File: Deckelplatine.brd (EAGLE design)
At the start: 160 x 100 mm, 57 parts, among them IC1 MAX481CSA, IC2 74HCT595D, IC3 74HCT595D, IC4 74HCT595D, IC5 74HCT595D, IC6 74HCT595D, J1 CON25, U1 LM2676S, X1 ''

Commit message: Begin mit dem Board Layout
Erste Lieferung von Farnell angekommen.
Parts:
- J1: value CON25 -> 52808-2570; device RA-GAS Projekte LTD:CON25 -> RA-GAS Projekte LTD:52808-2570
- moved R2 172.9 mm to (93.0, 7.00), turned to 90 degrees
- moved IC1 159.9 mm to (83.1, 69.0), turned to 270 degrees
- moved R4 159.3 mm to (70.9, 4.42), turned to 180 degrees
- moved C4 153.1 mm to (91.1, 29.2)
- moved D2 147.7 mm to (71.2, 13.9), turned to 90 degrees
- moved X1 146.6 mm to (103.4, 10.3), turned to 270 degrees
- moved F1 135.1 mm to (101.6, 29.2), turned to 270 degrees
- moved D1 133.4 mm to (64.5, 15.8), turned to 180 degrees
- moved IC3 132.4 mm to (68.5, 65.3), turned to 90 degrees
- moved JP3 131.5 mm to (104.1, 58.9), turned to 90 degrees
- moved R1 124.8 mm to (93.0, 12.8), turned to 90 degrees
- moved R15 123.2 mm to (40.0, 30.5), turned to 90 degrees
- moved JP2 122.2 mm to (95.3, 67.4)
- moved R14 118.2 mm to (41.0, 34.0), turned to 90 degrees
- moved IC2 115.9 mm to (68.5, 53.5), turned to 90 degrees
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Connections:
- net BETRIEB: now also J1.21; no longer J1.P$21
- net BLINK: now also J1.24; no longer J1.P$24
- net D1: now also J1.1; no longer J1.P$1
- net D17: now also J1.17; no longer J1.P$17
- net D18: now also J1.18; no longer J1.P$18
- net D19: now also J1.19; no longer J1.P$19
- net D2: now also J1.2; no longer J1.P$2
- net D20: now also J1.20; no longer J1.P$20
- net D3: now also J1.3; no longer J1.P$3
- net D4: now also J1.4; no longer J1.P$4
- net D5: now also J1.5; no longer J1.P$5
- net D6: now also J1.6; no longer J1.P$6
- net D7: now also J1.7; no longer J1.P$7
- net D8: now also J1.8; no longer J1.P$8
- net GND: now also J1.25; no longer J1.P$25
- net N$31: now also J1.9; no longer J1.P$9
- net N$32: now also J1.10; no longer J1.P$10
- net N$33: now also J1.11; no longer J1.P$11
- net N$34: now also J1.12; no longer J1.P$12
- net N$35: now also J1.13; no longer J1.P$13
- net N$36: now also J1.14; no longer J1.P$14
- net N$37: now also J1.15; no longer J1.P$15
- net N$38: now also J1.16; no longer J1.P$16
- net STOERUNG: now also J1.22; no longer J1.P$22
- net WARTUNG: now also J1.23; no longer J1.P$23
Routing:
- net TXD: track 0.00 -> 130.1 mm
- net MON_MAINS: track 0.00 -> 101.4 mm
- net 12V_VIN: track 0.00 -> 12.4 mm
- net GND: track 0.00 -> 1.03 mm
- net VCC: track 0.00 -> 0.56 mm
- added copper zone on layer 1, net GND
- added copper zone on layer 16, net GND
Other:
- board size 160 x 100 mm -> 110 x 75 mm

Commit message: Stromlaufplan fast fertig.
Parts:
- added X2: 233-502, con-wago_233:P-233-502
- C1, C10, C7, C8, C9: device rcl:C1206 -> resistor:C0603
- C11: value 0.1uF -> 100n; device rcl:C1206 -> resistor:C0603
- C4: value 0.01uF -> 0.1uF; device rcl:C0805 -> rcl:C1206
- C5: value 100uF 16v -> 0.01uF; device rcl:PANASONIC_D -> rcl:C0805
- C6: value 100n -> 100uF 16v; device rcl:C1206 -> rcl:PANASONIC_D
- F1: device fuse:KS9V -> fuse-schurter:3101.0040
- IC1: value MAX481CSA -> MAX1487EESA+
- JP1: value CON6 -> ''
- L1: value 09HCP33UH -> DO5022P-EU_; device Inductor-Fastron:09HCP -> RA-GAS Projekte LTD:DO5022P
- X1: value '' -> 236-404; device con-wago:233-504 -> con-wago_236:P-236-404
- moved C1 83.4 mm to (92.8, 61.0), turned to 0 degrees
- moved C7 82.9 mm to (74.7, 72.2), turned to 0 degrees
- moved C3 67.4 mm to (85.0, 25.0), turned to 270 degrees
- moved C2 65.4 mm to (88.0, 25.0), turned to 270 degrees
- moved R2 65.1 mm to (28.0, 4.00)
- moved R1 65.0 mm to (28.0, 11.0)
- moved IC3 55.1 mm to (13.4, 66.7), turned to 270 degrees
- moved C8 48.9 mm to (73.9, 59.2), turned to 0 degrees
- moved IC2 46.0 mm to (24.4, 66.5), turned to 270 degrees
- moved C6 40.5 mm to (56.3, 19.0)
- moved R4 36.9 mm to (34.0, 4.00), turned to 90 degrees
- moved R3 31.5 mm to (34.0, 11.0), turned to 90 degrees
- moved C11 28.4 mm to (27.0, 31.0), turned to 270 degrees
- moved U1 28.2 mm to (87.9, 44.0), turned to 270 degrees
- moved F1 23.4 mm to (83.6, 14.2)
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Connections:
- net BETRIEB renamed D21
- net BLINK renamed D24
- net N$31 renamed D9
- net N$32 renamed D10
- net N$33 renamed D11
- net N$34 renamed D12
- net N$35 renamed D13
- net N$36 renamed D14
- net N$37 renamed D15
- net N$38 renamed D16
- net STOERUNG renamed D22
- net WARTUNG renamed D23
- new net N$31: F1.3, F1.4
- net 12V_VIN: now also C4.1, X1.L1.1, X1.L1.2; no longer C11.1, X1.B1
- net ACCU+: now also F1.2, X1.L3.1, X1.L3.2; no longer X1.B3
- net ACCU-: now also X1.L4.1, X1.L4.2; no longer X1.B4
- net GND: now also C4.2, C6.-, X1.L2.1, X1.L2.2, X2.L2.1, X2.L2.2; no longer C5.-, C6.2, X1.B2
- net N$1: no longer F1.2
- net N$42: now also C5.2; no longer C4.2
- net N$44: now also C5.1, L1.1; no longer C4.1, L1.P$2
- net VCC: now also C11.1, C6.+, L1.2, X2.L1.1, X2.L1.2; no longer C5.+, C6.1, L1.P$1
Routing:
- net TXD: track 130.1 -> 0.00 mm
- net MON_MAINS: track 101.4 -> 0.00 mm
- net 12V_VIN: track 12.4 -> 0.00 mm
- net VCC: track 0.56 -> 0.00 mm

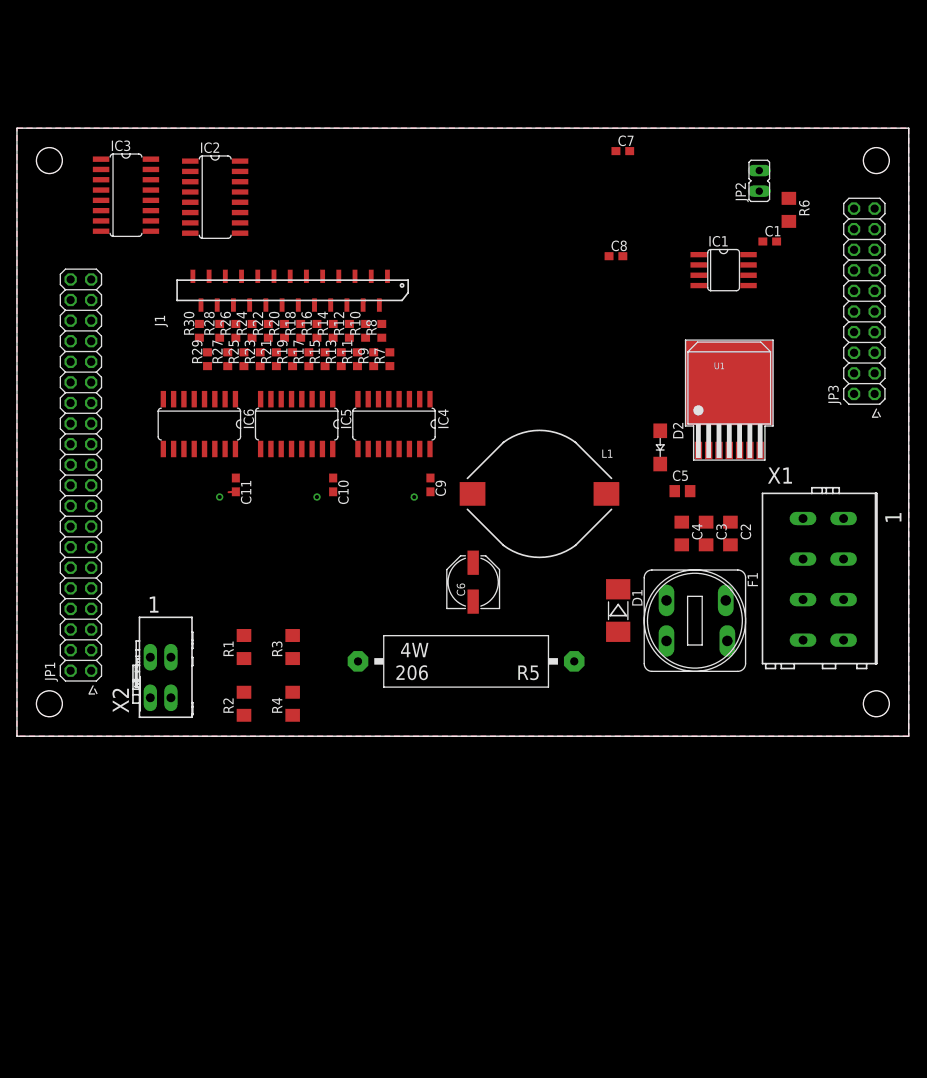
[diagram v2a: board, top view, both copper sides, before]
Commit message: Schema mit Verpolschutz an Vin und Accu.
Schaltregler nach Application Note von Texas Instruments.
Eingänge für den MON_MAINS und MON_BAT (GPIO Banana Pro Eingänge zur Überwachung Vin und Accu) sind durch NPN Transistoren gegen Überspannunge geschützt
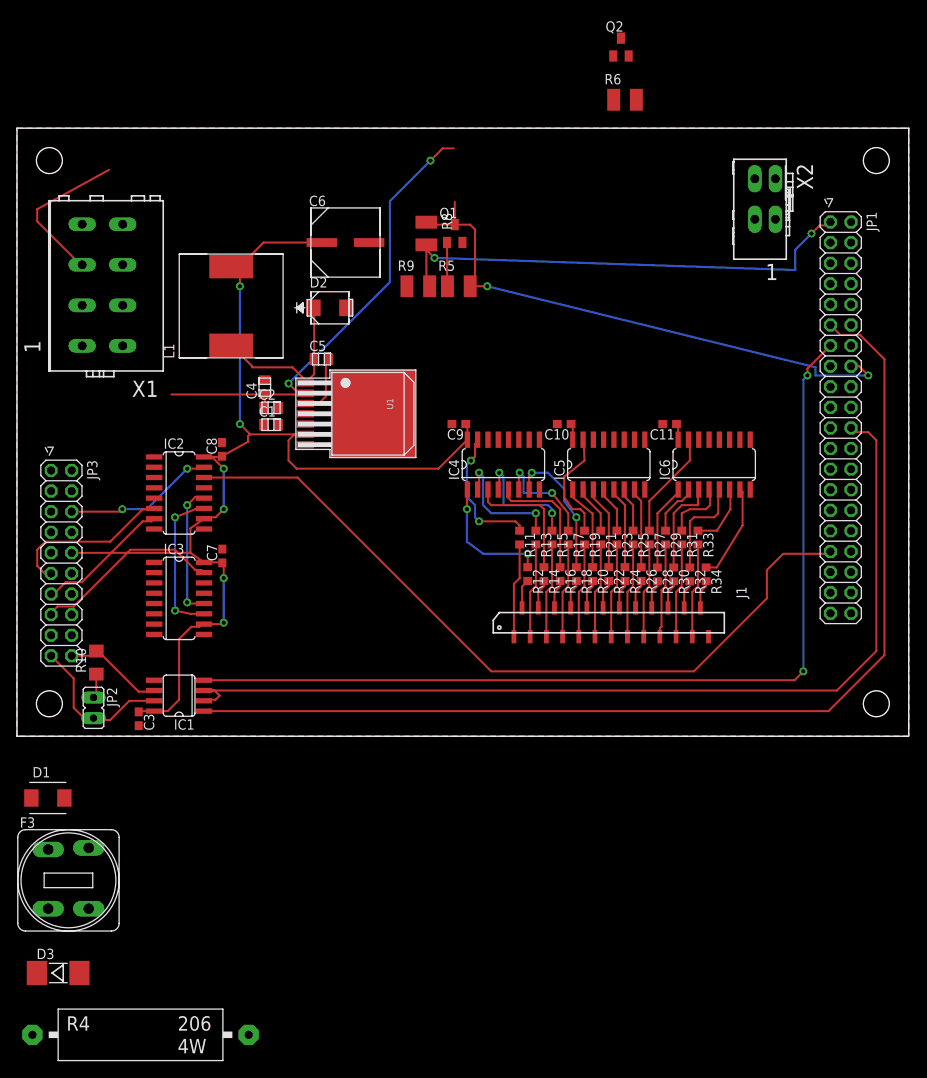
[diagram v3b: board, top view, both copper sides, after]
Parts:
- removed F1: 0.63AT, fuse-schurter:3101.0040
- removed R1, R3: 20k, rcl:R1206
- removed R2: 3.3k, rcl:R1206
- removed R7: 2.2k, RA-GAS Projekte LTD:R0603
- added D3: LL4005G, diode:MELF-MLL41
- added F3: 0.63AT, fuse-schurter:3101.0040
- added Q1, Q2: BC846BSMD, transistor-npn:SOT23
- added R31, R32, R33, R34: 2.2k, RA-GAS Projekte LTD:R0603
- C1: value 100n -> 0.1uF; device resistor:C0603 -> AcceleratedDesigns_Lib:GRM21BR61E475MA12L
- C2: device rcl:C1206 -> AcceleratedDesigns_Lib:GRM21BR61E475MA12L
- C3: value 0.1uF -> 100n; device rcl:C1206 -> resistor:C0603
- C4: device rcl:C1206 -> AcceleratedDesigns_Lib:0805
- C5: device rcl:C0805 -> AcceleratedDesigns_Lib:GRM216R71H103KA01D
- C6: device rcl:PANASONIC_D -> AcceleratedDesigns_Lib:SM_RADIAL_8MM
- D1: value LL4005G -> (none); device diode:MELF-MLL41 -> diode:SMBJ
- D2: value GF1 -> 450mV; device diode:SMA-DO214AC -> AcceleratedDesigns_Lib:SMB
- L1: value DO5022P-EU_ -> SRR1280-150M; device RA-GAS Projekte LTD:DO5022P -> AcceleratedDesigns_Lib:SRR1280
- R10: value 2.2k -> 120R; device RA-GAS Projekte LTD:R0603 -> rcl:R1206
- R4: value 3.3k -> 150R RMO3E150; device rcl:R1206 -> resistor-power:KH206-8
- R5: value 150R RMO3E150 -> 1k; device resistor-power:KH206-8 -> rcl:R1210
- R6: value 120R -> 1k; device rcl:R1206 -> rcl:R1210
- R8, R9: value 2.2k -> 10k; device RA-GAS Projekte LTD:R0603 -> rcl:R1210
- moved JP2 104.7 mm to (9.44, 3.50), turned to 180 degrees
- moved JP3 104.2 mm to (5.48, 21.4), turned to 270 degrees
- moved X1 95.1 mm to (11.0, 55.5), turned to 180 degrees
- moved JP1 94.0 mm to (101.6, 39.3), turned to 270 degrees
- moved X2 93.1 mm to (92.0, 65.0), turned to 270 degrees
- moved IC1 85.2 mm to (20.0, 5.00), turned to 90 degrees
- moved D1 74.1 mm to (3.81, -7.62), turned to 0 degrees
- moved C3 73.6 mm to (15.0, 2.15)
- moved C7 70.2 mm to (25.3, 22.2), turned to 90 degrees
- moved R30 65.8 mm to (81.0, 20.0), turned to 270 degrees
- moved C1 65.5 mm to (31.3, 38.4)
- moved IC6 63.7 mm to (86.0, 33.5), turned to 0 degrees
- moved R28 61.8 mm to (79.0, 20.0), turned to 270 degrees
- moved R29 60.6 mm to (80.0, 24.5), turned to 270 degrees
- moved C2 58.7 mm to (31.3, 40.5), turned to 0 degrees
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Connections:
- removed net MON_BAT: JP1.18, R3.1, R4.2
- removed net MON_MAINS: JP1.16, R1.1, R2.2
- removed net N$1: D1.A, R3.2, R5.1
- removed net N$31: F1.3, F1.4
- new net !MON_BAT: JP1.18, Q2.3, R6.2, R9.1
- new net !MON_MAINS: JP1.16, Q1.3, R5.2, R8.1
- new net N$37: Q1.1, R5.1
- new net N$38: D3.A, F3.4, R4.1
- new net N$39: F3.1
- new net N$4: Q2.1, R6.1
- new net V+: D3.C, R4.2
- net 12V_VIN: now also C1.1, D1.A; no longer C3.1, R1.2, R5.2
- net A-: now also R10.2; no longer R6.2
- net ACCU+: no longer F1.1, F1.2
- net ACCU-: no longer R4.1
- net D1: now also R11.2; no longer R7.2
- net D10: now also R20.2; no longer R16.2
- net D11: now also R21.2; no longer R17.2
- net D12: now also R22.2; no longer R18.2
- net D13: now also R23.2; no longer R19.2
- net D14: now also R24.2; no longer R20.2
- net D15: now also R25.2; no longer R21.2
- net D16: now also R26.2; no longer R22.2
- net D17: now also R27.2; no longer R23.2
- net D18: now also R28.2; no longer R24.2
- net D19: now also R29.2; no longer R25.2
- net D2: now also R12.2; no longer R8.2
- net D20: now also R30.2; no longer R26.2
- net D21: now also R31.2; no longer R27.2
- net D22: now also R32.2; no longer R28.2
- net D23: now also R33.2; no longer R29.2
- net D24: now also R34.2; no longer R30.2
- net D3: now also R13.2; no longer R9.2
- net D4: now also R14.2; no longer R10.2
- net D5: now also R15.2; no longer R11.2
- net D6: now also R16.2; no longer R12.2
- net D7: now also R17.2; no longer R13.2
- net D8: now also R18.2; no longer R14.2
- net D9: now also R19.2; no longer R15.2
- net GND: now also C6.2, D2.2, Q1.2, Q2.2; no longer C6.-, D2.A, R2.1
- net N$10: now also R15.1; no longer R11.1
- net N$11: now also R16.1; no longer R12.1
- net N$12: now also R17.1; no longer R13.1
- net N$13: now also R18.1; no longer R14.1
- net N$14: now also R19.1; no longer R15.1
- net N$15: now also R20.1; no longer R16.1
- net N$16: now also R21.1; no longer R17.1
- net N$17: now also R22.1; no longer R18.1
- net N$18: now also R10.1; no longer R6.1
- net N$19: now also R23.1; no longer R19.1
- net N$20: now also R24.1; no longer R20.1
- net N$21: now also R25.1; no longer R21.1
- net N$22: now also R26.1; no longer R22.1
- net N$23: now also R27.1; no longer R23.1
- net N$24: now also R28.1; no longer R24.1
- net N$25: now also R29.1; no longer R25.1
- net N$26: now also R30.1; no longer R26.1
- net N$27: now also R31.1; no longer R27.1
- net N$28: now also R32.1; no longer R28.1
- net N$29: now also R33.1; no longer R29.1
- net N$30: now also R34.1; no longer R30.1
- net N$44: now also D2.1; no longer D2.K
- net N$6: now also R11.1; no longer R7.1
- net N$7: now also R12.1; no longer R8.1
- net N$8: now also R13.1; no longer R9.1
- net N$9: now also R14.1; no longer R10.1
- net VCC: now also C3.1, C6.1; no longer C1.1, C6.+
- net VCC3.3V: now also R8.2, R9.2
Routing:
- net VCC: track 0.00 -> 144.8 mm, vias 0 -> 6
- net RXD: track 0.00 -> 131.7 mm
- net RTS: track 0.00 -> 118.9 mm
- net TXD: track 0.00 -> 115.9 mm, vias 0 -> 2
- net REL_SER: track 0.00 -> 95.3 mm
- net !MON_MAINS: track 0.00 -> 70.3 mm, vias 0 -> 2
- net VCC3.3V: track 0.00 -> 60.1 mm, vias 0 -> 2
- net 12V_VIN: track 0.00 -> 58.9 mm, vias 0 -> 2
- net P9: track 0.00 -> 23.5 mm
- net N$44: track 0.00 -> 21.1 mm
- net P7: track 0.00 -> 20.6 mm
- net ACCU+: track 0.00 -> 19.6 mm
- net B+: track 0.00 -> 19.1 mm
- net REL_SCK: track 0.00 -> 18.9 mm, vias 0 -> 2
- net P1: track 0.00 -> 18.6 mm, vias 0 -> 2
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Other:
- outline, holes or cut-outs redrawn

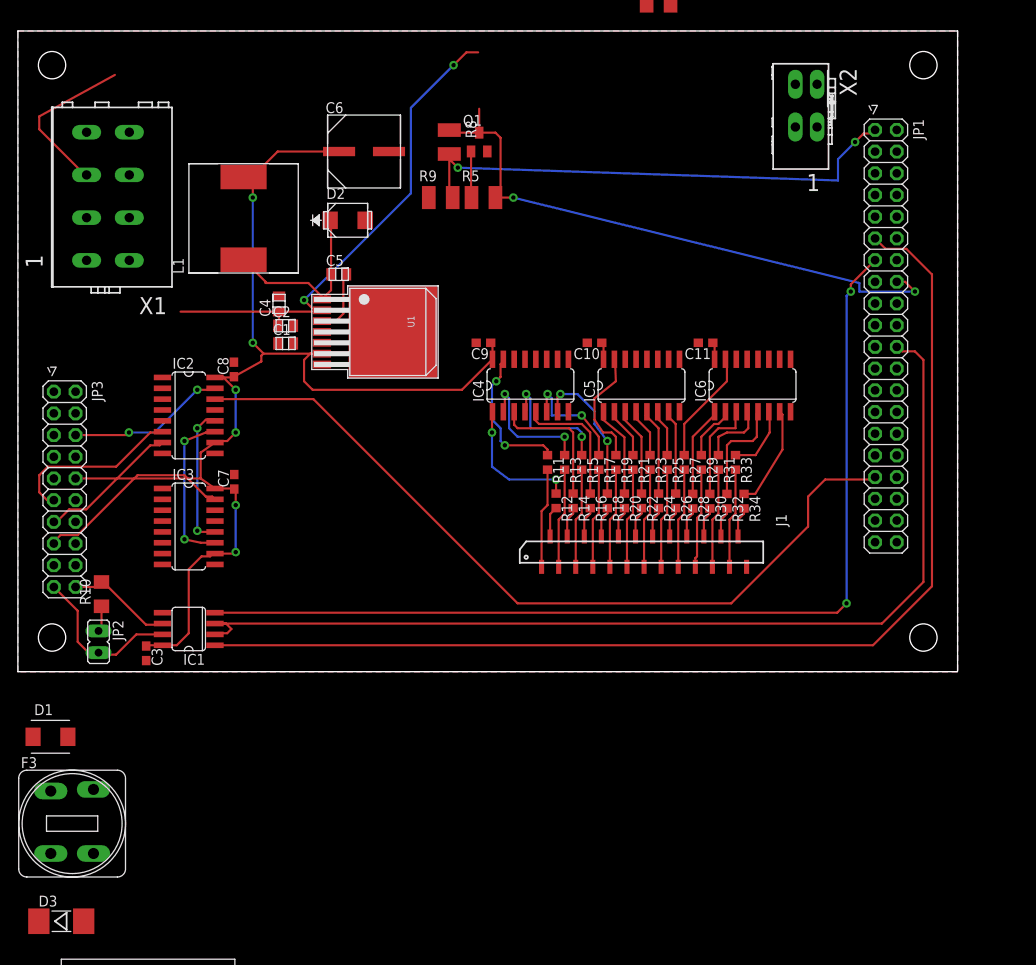
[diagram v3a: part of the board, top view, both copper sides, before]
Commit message: Widerstand 150Ohm, 4Watt ausgetauscht
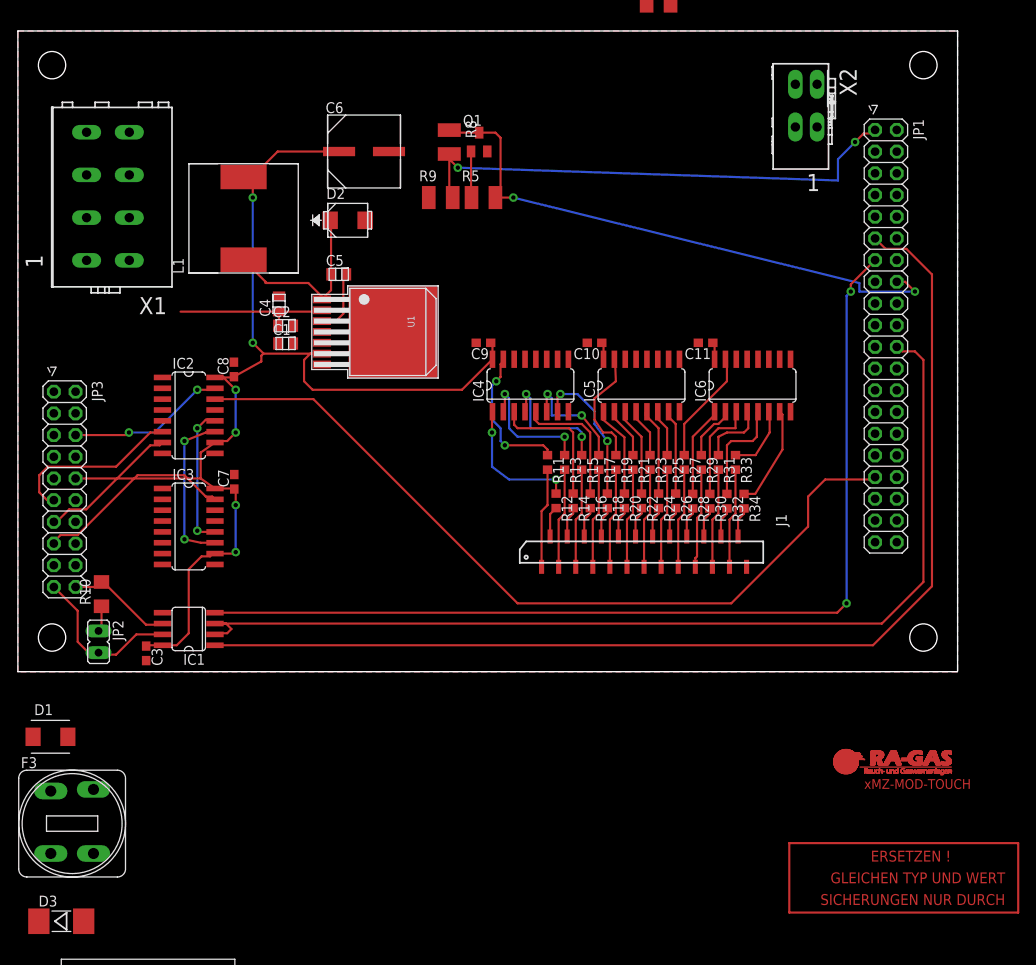
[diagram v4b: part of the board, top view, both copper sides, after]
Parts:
- D1: value (none) -> SSB44
- R4: value 150R RMO3E150 -> 150R, 4W, 5%
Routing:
- net N$1413: track 0.00 -> 69.8 mm
- net 12V_VIN: track 58.9 -> 18.1 mm, vias 2 -> 0
- net ACCU+: track 19.6 -> 0.00 mm
- net N$778: track 0.00 -> 10.7 mm
- net !MON_MAINS: track 70.3 -> 67.5 mm
- net N$790: track 0.00 -> 2.77 mm
- net N$787: track 0.00 -> 2.77 mm
- net N$1323: track 0.00 -> 2.77 mm
- net N$786: track 0.00 -> 2.74 mm
- net N$785: track 0.00 -> 2.72 mm
- net N$784: track 0.00 -> 2.72 mm
- net N$1329: track 0.00 -> 2.69 mm
- net N$783: track 0.00 -> 2.67 mm
- net N$782: track 0.00 -> 2.67 mm
- net N$781: track 0.00 -> 2.67 mm
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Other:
- board text added: "ERSETZEN !"
- board text added: "GLEICHEN TYP UND WERT"
- board text added: "SICHERUNGEN NUR DURCH"
- board text added: "xMZ-MOD-TOUCH"
